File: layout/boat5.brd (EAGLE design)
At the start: 100 x 80 mm, 74 parts, among them IC3 ATMEGA2560-16AU, Q1 60V, Q2 60V, U1 MPU-9150, U2 VENUS638FLPX-L, U3 USD-SOCKETNEW, Y1 CSTCE16M0V53-R0 16MHZ

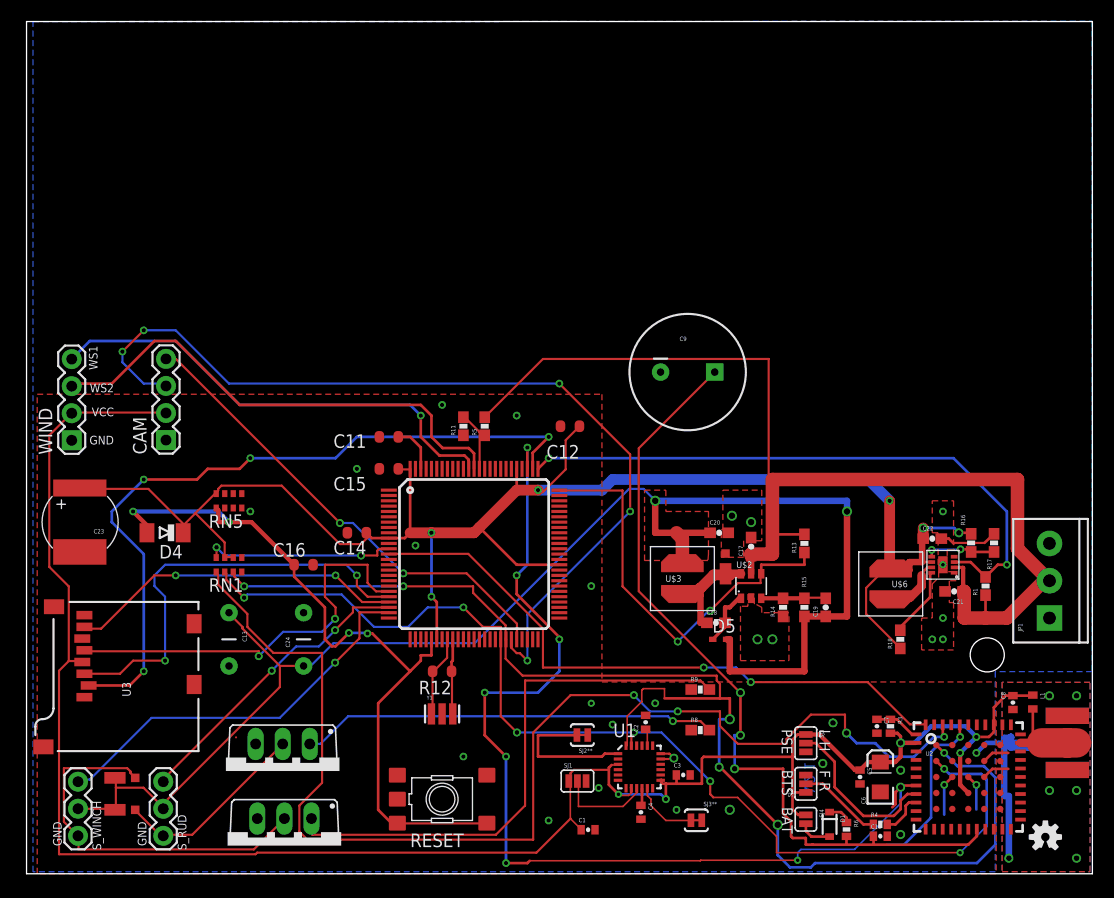
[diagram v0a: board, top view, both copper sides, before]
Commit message: first pass at routing
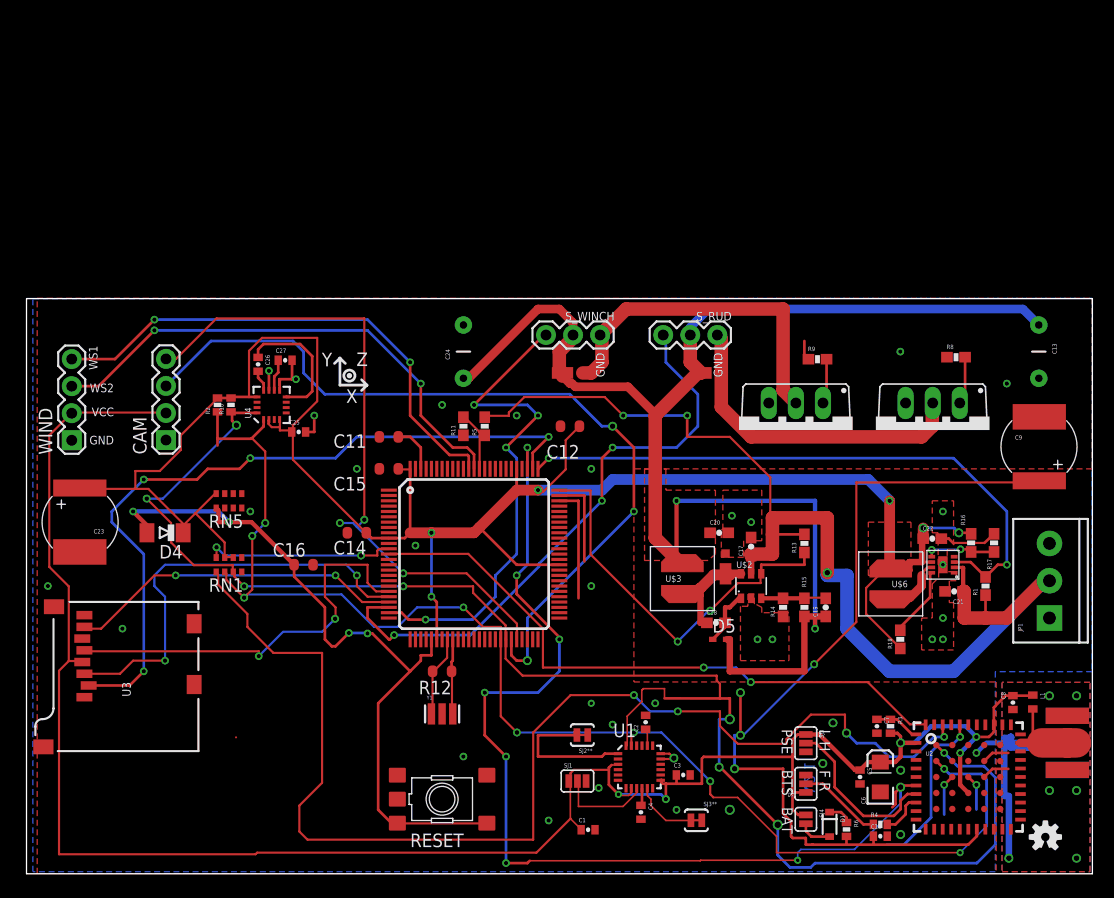
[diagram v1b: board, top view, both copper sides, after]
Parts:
- added C25: .1uF, SparkFun:0402-CAP
- added C26: .22uF, SparkFun:0402-CAP
- added C27: 4.7uF, SparkFun:0402-CAP
- added R10, R2: DNP, SparkFun:0402-RES
- added U4: HMC5883LSMD, SparkFun:16LPCC
- C9: device SparkFun:CPOL-RADIAL-1000UF-25V -> SparkFun:EN_J2
- moved C13 80.7 mm to (95.0, 49.0)
- moved S_RUD 70.1 mm to (64.8, 50.6), turned to 180 degrees
- moved Q2 68.9 mm to (85.0, 41.6)
- moved D$2 68.6 mm to (64.0, 47.0)
- moved S_WINCH 67.9 mm to (53.8, 50.6), turned to 180 degrees
- moved Q1 61.8 mm to (72.2, 41.6)
- moved D$1 56.6 mm to (51.0, 47.0)
- moved R8 42.4 mm to (87.2, 48.5)
- moved C9 33.7 mm to (95.0, 40.1)
- moved R9 32.9 mm to (74.2, 48.3)
- moved C24 30.9 mm to (41.0, 49.0)
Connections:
- removed net PA4: IC3.74
- removed net PA5: IC3.73
- new net N$13: C26.2, U4.12
- new net N$16: C27.1, U4.10
- new net N$3: C26.1, U4.8
- net GND: now also C25.2, C27.2, C9.-, U4.11, U4.9; no longer C9.2
- net RUD_EN: now also IC3.74
- net SCL: now also R2.1, U4.1
- net SDA: now also R10.1, U4.16
- net VBAT: now also C9.+; no longer C9.1
- net VCC: now also C25.1, R10.2, R2.2, U4.13, U4.2, U4.4
- net WINCH_EN: now also IC3.73
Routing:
- net N$10: track 52.0 -> 4.25 mm
- net VCC: track 159.0 -> 195.5 mm
- net N$7: track 39.1 -> 4.51 mm, vias 1 -> 0
- net SDA: track 122.1 -> 149.6 mm, vias 6 -> 8
- net RUD_V: track 28.4 -> 55.5 mm, vias 2 -> 3
- net SCL: track 103.3 -> 128.3 mm, vias 7 -> 9
- net TXD1: track 44.7 -> 63.0 mm, vias 2 -> 3
- net WINCH_EN: track 0.00 -> 13.0 mm
- net N$3: track 0.00 -> 12.5 mm
- net N$9: track 18.5 -> 30.5 mm
- net GND: track 11.1 -> 20.8 mm, vias 28 -> 35
- net WN_V: track 37.2 -> 46.5 mm, vias 1 -> 4
- net VBAT: track 76.6 -> 85.4 mm, vias 3 -> 4
- net RUD_EN: track 0.00 -> 8.55 mm
- net RXD1: track 85.5 -> 78.3 mm, vias 5 -> 3
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- added copper zone on layer 1, net VCC
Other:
- board size 100 x 80 mm -> 100 x 54 mm
- board text added: "X"
- board text added: "Y"
- board text added: "Z"

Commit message: boat v5
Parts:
- removed Q2: 60V, transistor-power:TO220BV
- removed RN5: 10K, resistor-dil:CAT16
- added C28: 10nF, SparkFun-Passives:0402-CAP
- added J1: AVR_SPI_PRG_6PTH, SparkFun-Connectors:2X3
- added Q3, Q4: MOSFET-PCHANNELSMD, SparkFun-DiscreteSemi:SOT23-3
- added Q5, Q6: MOSFET-NCHANNELBSS138, SparkFun-DiscreteSemi:SOT23
- added R19: 10k, SparkFun-Resistors:0603-RES
- added R20, R21: 100k, SparkFun-Resistors:0603-RES
- added R22, R23, R24: 100R, SparkFun-Resistors:0603-RES
- Q1: value 60V -> MOSFET-NCHANNELBSS138; device transistor-power:TO220BV -> SparkFun-DiscreteSemi:SOT23
- moved JP5 95.4 mm to (2.32, 8.26), turned to 270 degrees
- moved U$4 91.9 mm to (4.38, 14.6)
- moved L1 90.0 mm to (5.56, 1.88), turned to 90 degrees
- moved C8 86.3 mm to (7.43, 1.94), turned to 90 degrees
- moved R7 84.0 mm to (8.13, 5.72), turned to 0 degrees
- moved C9 81.7 mm to (16.0, 19.1), turned to 90 degrees
- moved U2 76.8 mm to (11.6, 8.92), turned to 180 degrees
- moved R3 62.9 mm to (18.9, 4.16), turned to 90 degrees
- moved C10 61.2 mm to (19.9, 14.5), turned to 180 degrees
- moved R4 60.9 mm to (19.9, 13.4), turned to 180 degrees
- moved C7 60.4 mm to (20.2, 4.16), turned to 90 degrees
- moved C6 60.3 mm to (19.9, 8.92), turned to 270 degrees
- moved C5 56.4 mm to (21.8, 8.92), turned to 90 degrees
- moved R6 54.8 mm to (23.1, 13.8), turned to 90 degrees
- moved D1 51.5 mm to (24.6, 13.4), turned to 90 degrees
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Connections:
- removed net PC6: IC3.59
- removed net PC7: IC3.60
- removed net RX1: U2.52
- removed net TX1: U2.57
- removed net VCC: C12.1, C14.1, C15.1, C22.1, C23.+, C25.1, D4.C, IC3.10, IC3.100, IC3.31, IC3.61, IC3.80, R10.2, R16.2, R18.1, R2.2, RN1.6, RN1.7, RN5.8, U$1.P6, U$6.P$2, U4.13, U4.2, U4.4
- new net CAM_EN: IC3.59, R23.2
- new net GPS_EN: IC3.60, R22.2
- new net GPS_PWR: C5.1, C6.A, C8.1, L1.1, Q3.3, R3.2, SJ2.1, SJ3.1, SJ4.1, U2.2, U2.36, U2.58
- new net N$20: CAM.2, Q4.3
- new net N$21: Q4.1, R20.2, R23.1
- new net N$22: Q3.1, R21.2, R22.1
- new net N$23: Q1.3, R1.2, U$1.P3
- new net N$24: Q1.1, R24.2
- net 3.3V: now also C12.1, C14.1, C15.1, C22.1, C23.+, C25.1, C28.1, D4.C, IC3.10, IC3.100, IC3.31, IC3.61, IC3.80, J1.2, Q3.2, Q4.2, R10.2, R16.2, R18.1, R19.2, R2.2, R20.1, R21.1, RN1.6, RN1.7, U$1.P6, U$6.P$2, U4.13, U4.2, U4.4; no longer C5.1, C6.A, C8.1, CAM.2, L1.1, R3.2, SJ2.1, SJ3.1, SJ4.1, U2.2, U2.36, U2.58
- net GND: now also C28.2, J1.6, JP1.2, Q1.2, Q5.2, Q6.2, R13.2; no longer JP1.1, Q1.S, Q2.S
- net MISO: now also J1.1
- net MOSI: now also J1.4
- net N$10: now also Q6.1; no longer Q1.G
- net N$7: now also Q5.1; no longer Q2.G
- net N$8: now also Q6.3; no longer Q1.D
- net N$9: now also Q5.3; no longer Q2.D
- net RESET: now also J1.5, R19.1; no longer RN5.1
- net SCK: now also J1.3
- net SCL: no longer U2.46
- net SDA: no longer U2.45
- net VCC_EN: now also R24.1; no longer R1.2, U$1.P3
- net V_BATT: now also JP1.1; no longer JP1.2, R13.2
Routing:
- net VCC: track 195.5 -> 0.00 mm, vias 6 -> 0
- net 3.3V: track 189.7 -> 309.3 mm, vias 5 -> 15
- net SDA: track 149.6 -> 64.5 mm, vias 8 -> 5
- net VBAT: track 85.4 -> 19.1 mm, vias 4 -> 0
- net RX0: track 113.1 -> 47.5 mm
- net SCL: track 128.3 -> 67.4 mm, vias 9 -> 4
- net GPS_PWR: track 0.00 -> 57.2 mm, vias 0 -> 3
- net CAM_EN: track 0.00 -> 54.3 mm, vias 0 -> 2
- net WN_V: track 46.5 -> 85.2 mm, vias 4 -> 2
- net RXD1: track 78.3 -> 45.9 mm, vias 3 -> 1
- net GPS_EN: track 0.00 -> 30.3 mm, vias 0 -> 2
- net RUD_EN: track 8.55 -> 38.7 mm, vias 0 -> 4
- net N$8: track 32.3 -> 5.74 mm
- net N$9: track 30.5 -> 6.72 mm
- net VCC_EN: track 57.6 -> 37.0 mm
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- added copper zone on layer 1, net 3.3V
- added copper zone on layer 1, net V_BATT
- removed copper zone on layer 1, net VCC
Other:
- board size 100 x 54 mm -> 93 x 54 mm
- board text removed: "BAT"
- board text removed: "BTS"
- board text removed: "F R"
- board text removed: "L H"
- board text removed: "PSE"
- board text removed: "V2.1"

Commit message: board version 5.1
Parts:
- removed R10, R2: DNP, SparkFun:0402-RES
- removed R19: 10k, SparkFun-Resistors:0603-RES
- removed U$3: 4.7uH, kolosy:VLCF4020
- removed U$6: 15uH, kolosy:VLCF4020
- added C29: 0.1uF, SparkFun-Passives:0402-CAP
- added C30: (no value), kolosy:DSK-621
- added JP2: FTDI_DEVICE, SparkFun-Connectors:FTDI_DEVICE_SIDE
- added L2: 15uH, kolosy:VLCF4020
- added L3: 4.7uH, kolosy:SLFXXXX
- added R25: 70R, SparkFun-Resistors:0603-RES
- added STATUS: RED, SparkFun-LED:LED-0603
- C1, C2, C28, C3, C4: device SparkFun-Passives:0402-CAP -> SparkFun-Passives:0603-CAP
- C17, C20: device SparkFun-Capacitors:0603-CAP -> SparkFun-Capacitors:1206
- C18, C21, C22: device SparkFun-Capacitors:0603-CAP -> SparkFun-Capacitors:0805
- C23: value 200mF -> (none); device SparkFun-Capacitors:EN_J2 -> kolosy:DSK-621
- C25, C26, C27: device SparkFun:0402-CAP -> SparkFun:0603-CAP
- C9: value DNP -> 250uF; device SparkFun:EN_J2 -> SparkFun-Capacitors:CAP-PTH-5MM
- moved C9 60.0 mm to (73.0, 38.0)
- moved D4 17.5 mm to (48.0, 14.0), turned to 0 degrees
- moved R18 3.61 mm to (72.0, 24.0)
- moved C21 3.06 mm to (77.0, 26.7)
- moved C18 3.00 mm to (74.7, 5.55)
- moved C19 3.00 mm to (85.0, 7.00)
- moved C20 3.00 mm to (75.0, 14.0)
- moved C22 3.00 mm to (75.0, 31.4)
- moved D$3 3.00 mm to (75.6, 10.8)
- moved D5 3.00 mm to (75.0, 4.00)
- moved JP1 3.00 mm to (86.0, 24.0)
- moved R1 3.00 mm to (80.0, 27.0)
- moved R14 3.00 mm to (81.0, 7.00)
- moved R15 3.00 mm to (83.0, 7.00)
- moved R16 3.00 mm to (78.7, 31.1)
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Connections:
- removed net PC5: IC3.58
- removed net PE0: IC3.2
- removed net PE1: IC3.3
- removed net RX0: RN1.1, U2.42
- new net DTR: C29.1, JP2.P$1
- new net N$25: JP2.P$5
- new net N$27: R25.1, STATUS.C
- new net RX_D0: IC3.2, JP2.P$3
- new net STATUS_LED: IC3.58, STATUS.A
- new net TX_D0: IC3.3, JP2.P$2
- net 3.3V: now also C23.VCC, C9.1, JP2.P$4, L2.P$2, RN1.8; no longer C23.+, R10.2, R19.2, R2.2, U$6.P$2
- net 5V: now also L3.P$1; no longer U$3.P$1
- net GND: now also C23.GND, C30.GND, C9.2, JP2.P$6, R25.2; no longer C23.-, C9.-
- net N$12: now also L3.P$2; no longer U$3.P$2
- net N$14: now also L2.P$1; no longer U$6.P$1
- net RESET: now also C29.2, RN1.1; no longer R19.1
- net RXD2: now also U2.44; no longer RN1.8
- net SCL: no longer R2.1
- net SDA: no longer R10.1
- net TXD2: now also U2.42; no longer U2.44
- net VBAT: now also C30.VCC; no longer C9.+
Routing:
- net RESET: track 79.9 -> 141.8 mm, vias 3 -> 5
- net RX0: track 47.5 -> 0.00 mm, vias 4 -> 0
- net TX_D0: track 0.00 -> 45.1 mm, vias 0 -> 4
- net GND: track 16.2 -> 57.5 mm, vias 69 -> 98
- net RX_D0: track 0.00 -> 29.0 mm, vias 0 -> 3
- net RXD2: track 23.0 -> 45.1 mm
- net V_BATT: track 96.8 -> 105.9 mm
- net SCL: track 67.4 -> 60.6 mm
- net 5V: track 135.7 -> 141.5 mm
- net CAM_EN: track 54.3 -> 59.8 mm
- net TXD2: track 46.0 -> 50.9 mm
- net STATUS_LED: track 0.00 -> 4.31 mm
- net DTR: track 0.00 -> 3.92 mm
- net N$12: track 12.2 -> 15.6 mm
- net 5V_EN: track 56.7 -> 54.0 mm
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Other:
- board size 93 x 54 mm -> 89 x 54 mm
- board text added: "ARDUSAILOR V5.1"
- board text added: "RX_CAM"
- board text added: "TX_CAM"
- board text removed: "RX"
- board text removed: "TX"

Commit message: cleanup
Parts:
- removed SJ1: (no value), SparkFun-Passives:SJ_3_PASTE2&3
- removed SJ2**, SJ3**: SOLDERJUMPERTRACE, SparkFun-Passives:SJ_2S-TRACE
- R25: value 70R -> 100R
- moved C1 6.10 mm to (54.2, 11.1), turned to 90 degrees
- moved D$2 2.00 mm to (62.0, 47.0)
- moved R25 1.41 mm to (52.8, 22.9), turned to 180 degrees
- moved Q5 0.51 mm to (67.0, 48.0)
- moved R8 0.38 mm to (70.5, 48.0)
- moved C4 0.25 mm to (57.7, 5.27)
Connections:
- removed net AD0: SJ1.2, U1.9
- removed net CLKIN: SJ2**.2, U1.1
- removed net FSYNC: SJ3**.2, U1.11
- net 3.3V: no longer SJ1.1
- net GND: now also U$1.P_THERM_VIA1, U1.1, U1.11, U1.9; no longer SJ1.3, SJ2**.1, SJ3**.1
- net INT: now also IC3.66
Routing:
- net INT: track 0.00 -> 41.1 mm, vias 0 -> 2
- net GND: track 57.5 -> 25.6 mm
- net NAV: track 87.6 -> 56.1 mm, vias 6 -> 8
- net 5V: track 141.5 -> 125.6 mm
- net RESET: track 141.8 -> 126.4 mm, vias 5 -> 3
- net 3.3V: track 309.1 -> 296.0 mm
- net V_BATT: track 105.9 -> 97.1 mm
- net AD0: track 8.54 -> 0.00 mm
- net CLKIN: track 7.28 -> 0.00 mm
- net FSYNC: track 6.10 -> 0.00 mm
- net TX_D0: track 45.1 -> 41.1 mm
- net N$9: track 6.72 -> 7.99 mm
- net WINCH_EN: track 33.0 -> 33.8 mm
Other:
- board text added: "CAM_RX"
- board text added: "CAM_TX"
- board text removed: "RX_CAM"
- board text removed: "TX_CAM"

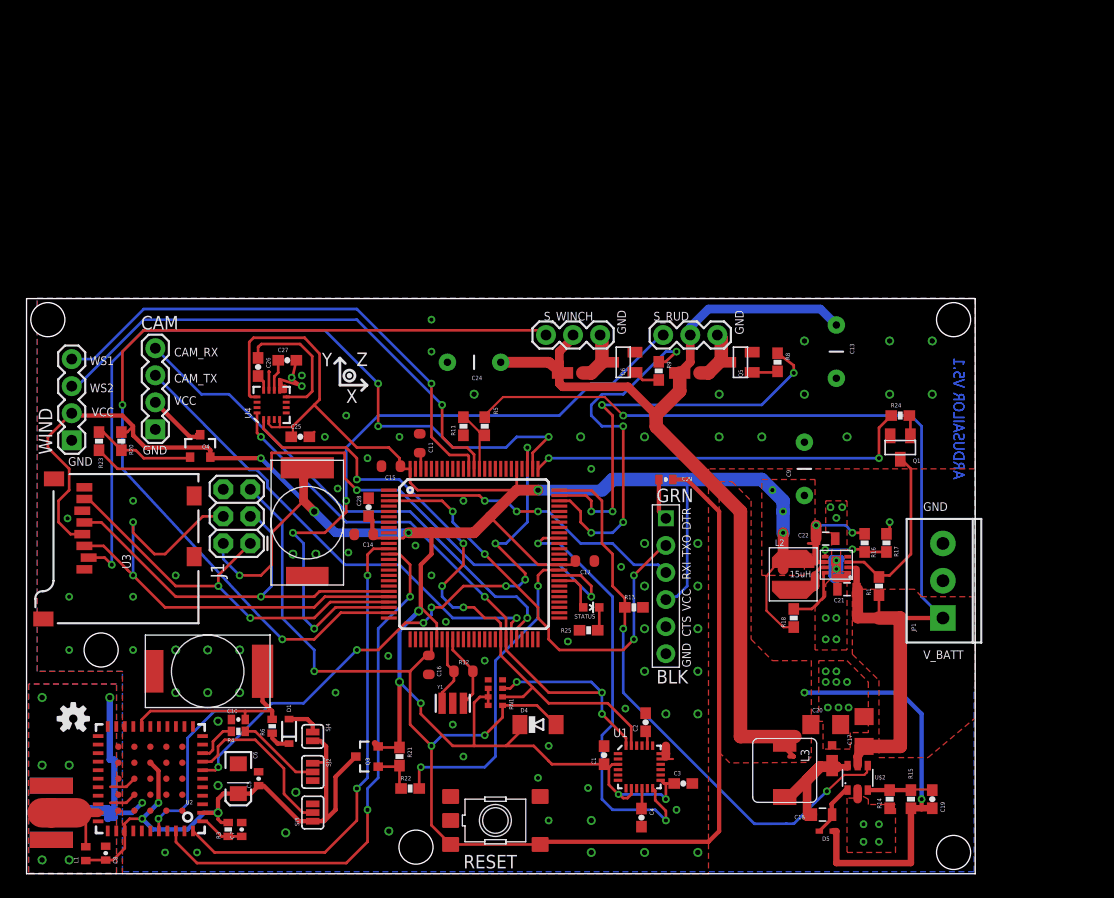
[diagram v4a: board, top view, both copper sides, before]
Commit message: 5.1 version final; 1A 5V reg
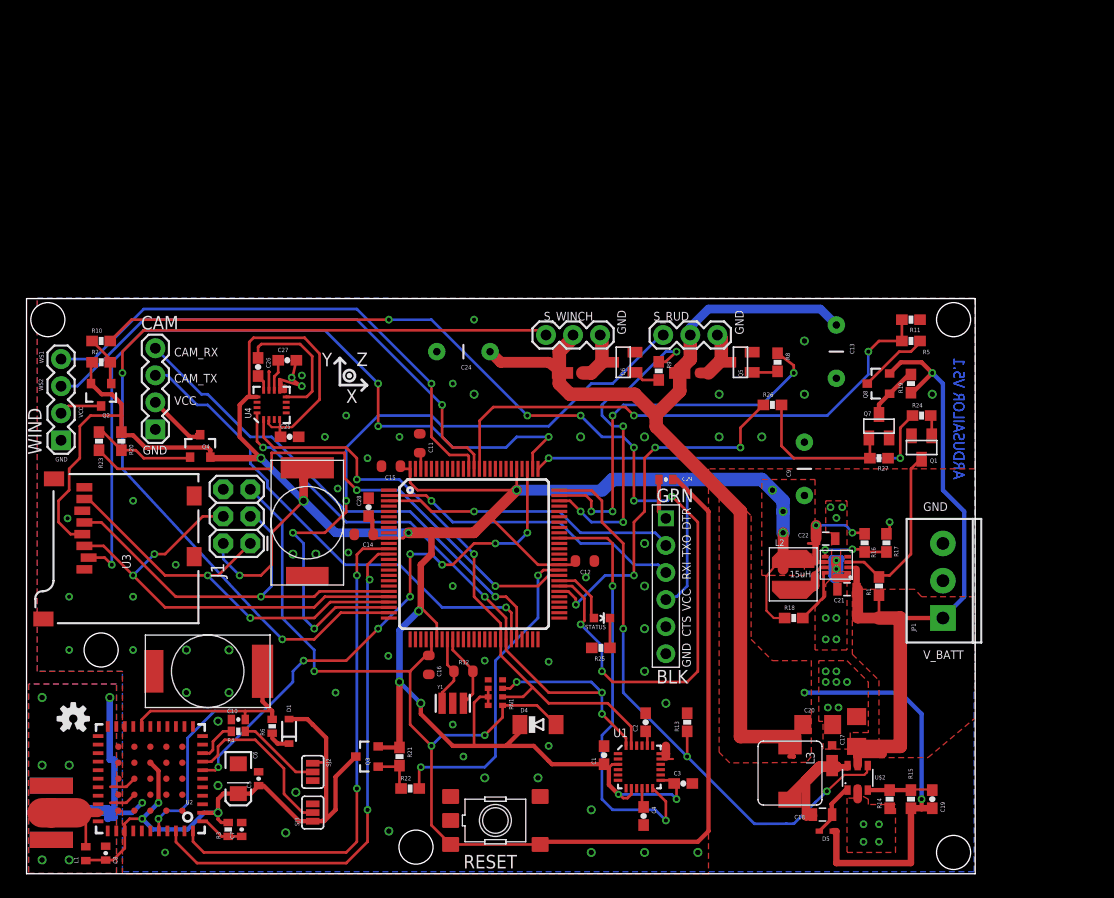
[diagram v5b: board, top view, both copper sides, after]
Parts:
- removed SJ4: BAT, SparkFun:SJ_2S
- added Q2, Q8: MOSFET-PCHANNELSMD, SparkFun-DiscreteSemi:SOT23-3
- added Q7: MOSFET-NCHANNELBSS138, SparkFun-DiscreteSemi:SOT23
- added R10, R26: 100R, SparkFun-Resistors:0603-RES
- added R19, R2, R27: 100k, SparkFun-Resistors:0603-RES
- C22: value 10uF -> 22uF
- R11: value 680R -> 100K
- R15: value 31.6k -> 56.2k
- R5: value 2.5K -> 324K
- moved R11 43.2 mm to (83.0, 52.0), turned to 180 degrees
- moved R5 40.8 mm to (83.0, 50.0), turned to 0 degrees
- moved R13 11.9 mm to (62.0, 14.2), turned to 90 degrees
- moved R25 2.01 mm to (53.9, 21.2)
- moved Q1 2.00 mm to (84.0, 40.0)
- moved R24 2.00 mm to (84.0, 43.0)
- moved C24 1.41 mm to (41.0, 49.0)
- moved STATUS 1.41 mm to (54.0, 24.0)
- moved C25 1.00 mm to (24.7, 41.0)
- moved WIND 1.00 mm to (3.24, 40.7)
- moved C20 0.75 mm to (74.2, 14.0)
- moved C17 0.70 mm to (77.9, 13.3)
- moved L3 0.56 mm to (71.7, 9.45)
- moved C4 0.25 mm to (57.9, 5.42)
- turned R18 to 0 degrees
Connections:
- removed net N$6: D1.2, SJ4.2
- removed net PC3: IC3.56
- removed net PC4: IC3.57
- new net BATT_SENS_EN: IC3.56, R26.1
- new net N$26: Q2.3, WIND.2
- new net N$28: Q2.1, R10.1, R2.2
- new net N$29: Q8.3, R5.2
- new net N$30: Q7.3, Q8.1, R19.2
- new net N$31: Q7.1, R26.2, R27.2
- new net WIND_EN: IC3.57, R10.2
- net 3.3V: now also Q2.2, R2.1; no longer WIND.2
- net GND: now also Q7.2, R27.1
- net GPS_PWR: now also D1.2; no longer SJ4.1
- net V_BATT: now also Q8.2, R19.1; no longer R5.2
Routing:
- net WIND_EN: track 0.00 -> 101.6 mm, vias 0 -> 8
- net V_BATT_DIV: track 6.79 -> 51.2 mm, vias 0 -> 2
- net BATT_SENS_EN: track 0.00 -> 34.7 mm, vias 0 -> 4
- net V_BATT: track 97.1 -> 70.8 mm
- net N$31: track 0.00 -> 14.6 mm
- net TX_D0: track 41.1 -> 27.8 mm, vias 4 -> 1
- net CAM_EN: track 59.8 -> 52.4 mm
- net N$29: track 0.00 -> 6.69 mm
- net NAV: track 56.1 -> 50.1 mm
- net MOSI: track 48.1 -> 42.1 mm
- net N$30: track 0.00 -> 5.11 mm
- net N$28: track 0.00 -> 4.75 mm
- net 3.3V: track 296.0 -> 291.6 mm
- net N$26: track 0.00 -> 4.04 mm
- net GPS_PWR: track 57.2 -> 60.7 mm
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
